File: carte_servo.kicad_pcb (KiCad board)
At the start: 4 copper layers, 185 x 106.7 mm, 134 parts, among them J10 Conn_01x03_Male, J11 Transistor_2, J12 Transistor_1, J13 Transistor_4, J14 Transistor_.3, J16 Conn_01x04_Male, J17 Conn_01x04_Male, J18 Conn_01x03_Male, J19 Conn_01x03_Male, J2 Conn_02x04_Top_Bottom, J20 Stepper, J21 Stepper, J24 Conn_LEDs, J25 Conn_AX12, J29 Conn_AX12, J5 Conn_01x03_Male, J6 Conn_01x03_Male, J7 Conn_01x03_Male, J8 Conn_01x03_Male, J9 Conn_01x03_Male, P1 USB_C_Plug_USB2.0, Q1 DMN2011UTS, Q2 DMN2011UTS, Q3 DMN2011UTS, Q4 DMN2011UTS, Q6 DMN2011UTS, Q7 CSD17307Q5A, Q8 CSD17579Q5A, SW1 CK_KMS2xxG, U1 XGZP6897D_differential_pressu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, U10 TPS563200, U2 XGZP6897D_differential_pressu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, U3 TMC2208_SILENTSTEPSTICK, U4 TMC2208_SILENTSTEPSTICK, U5 74LVC2G241, U6 SN65HVD230, U7 LD1117S33TR_SOT223, U8 ESP32-S3-WROOM-1, U9 LM3150MH

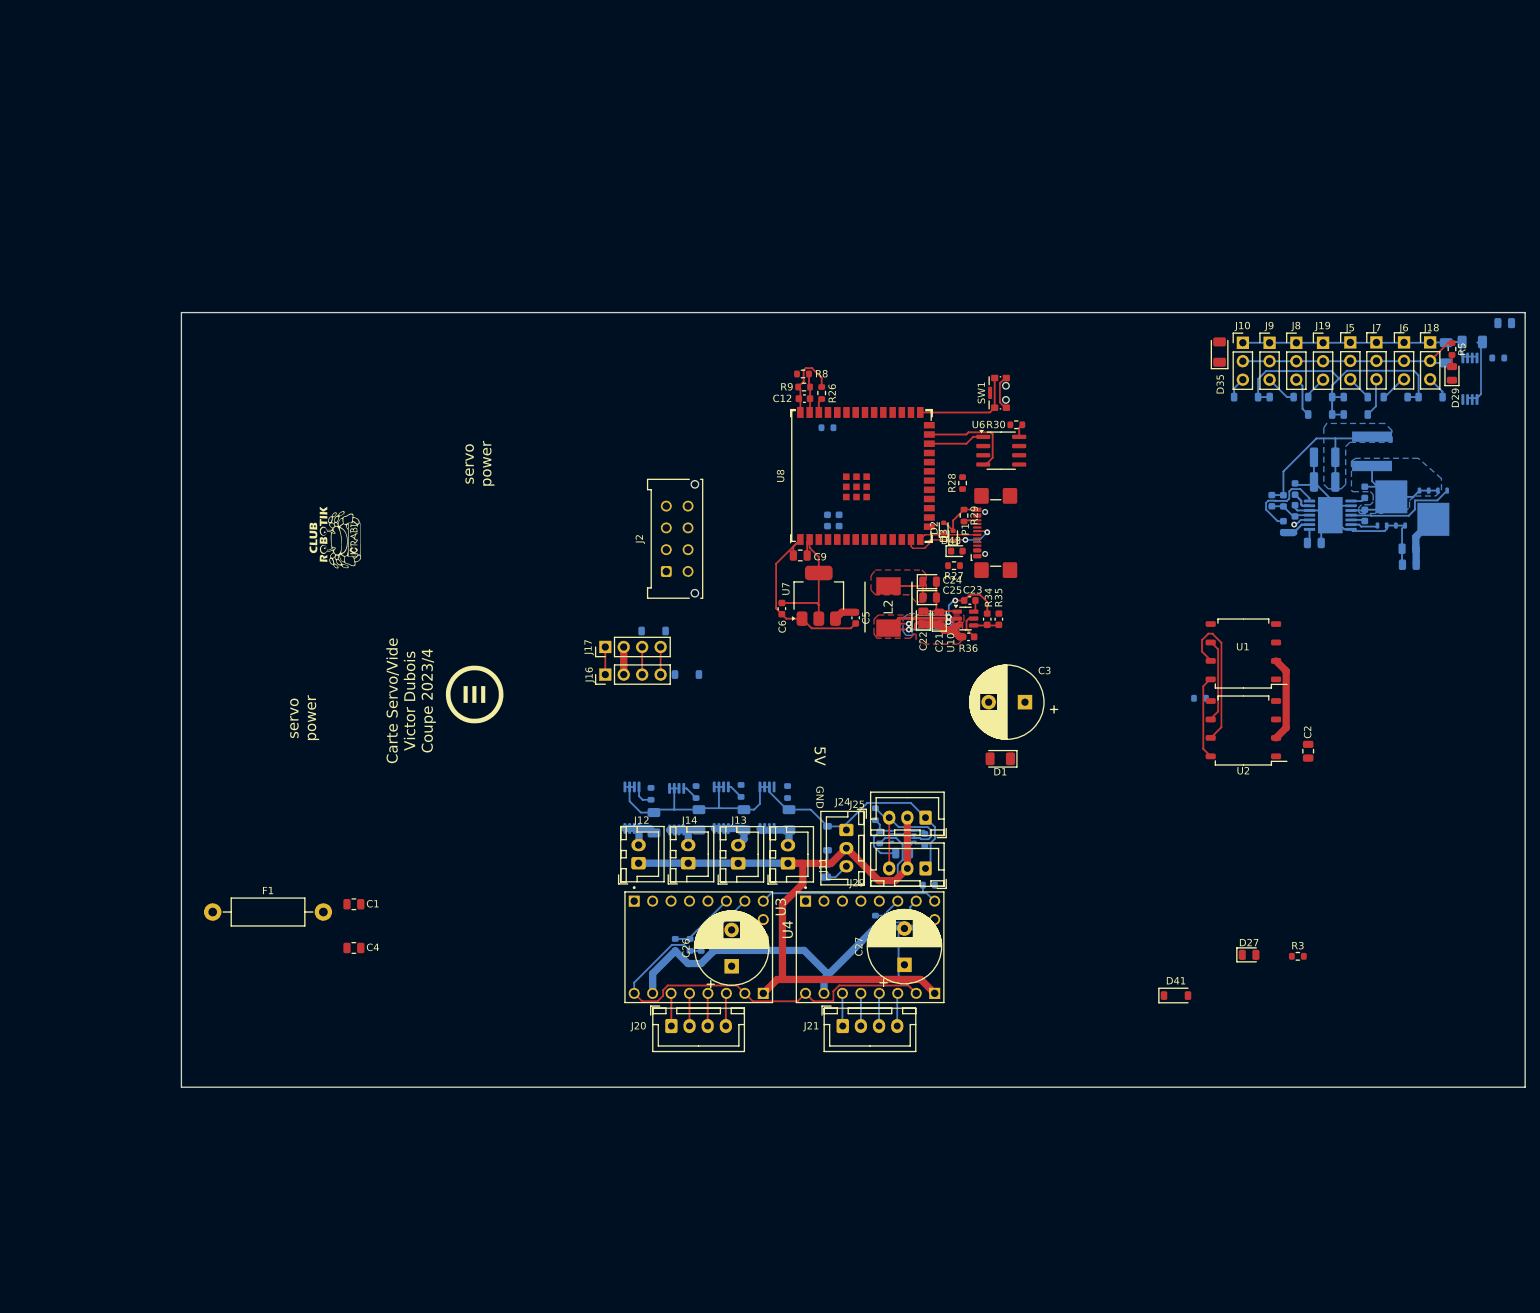
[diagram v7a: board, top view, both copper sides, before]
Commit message: change fuse + start servo order + routing
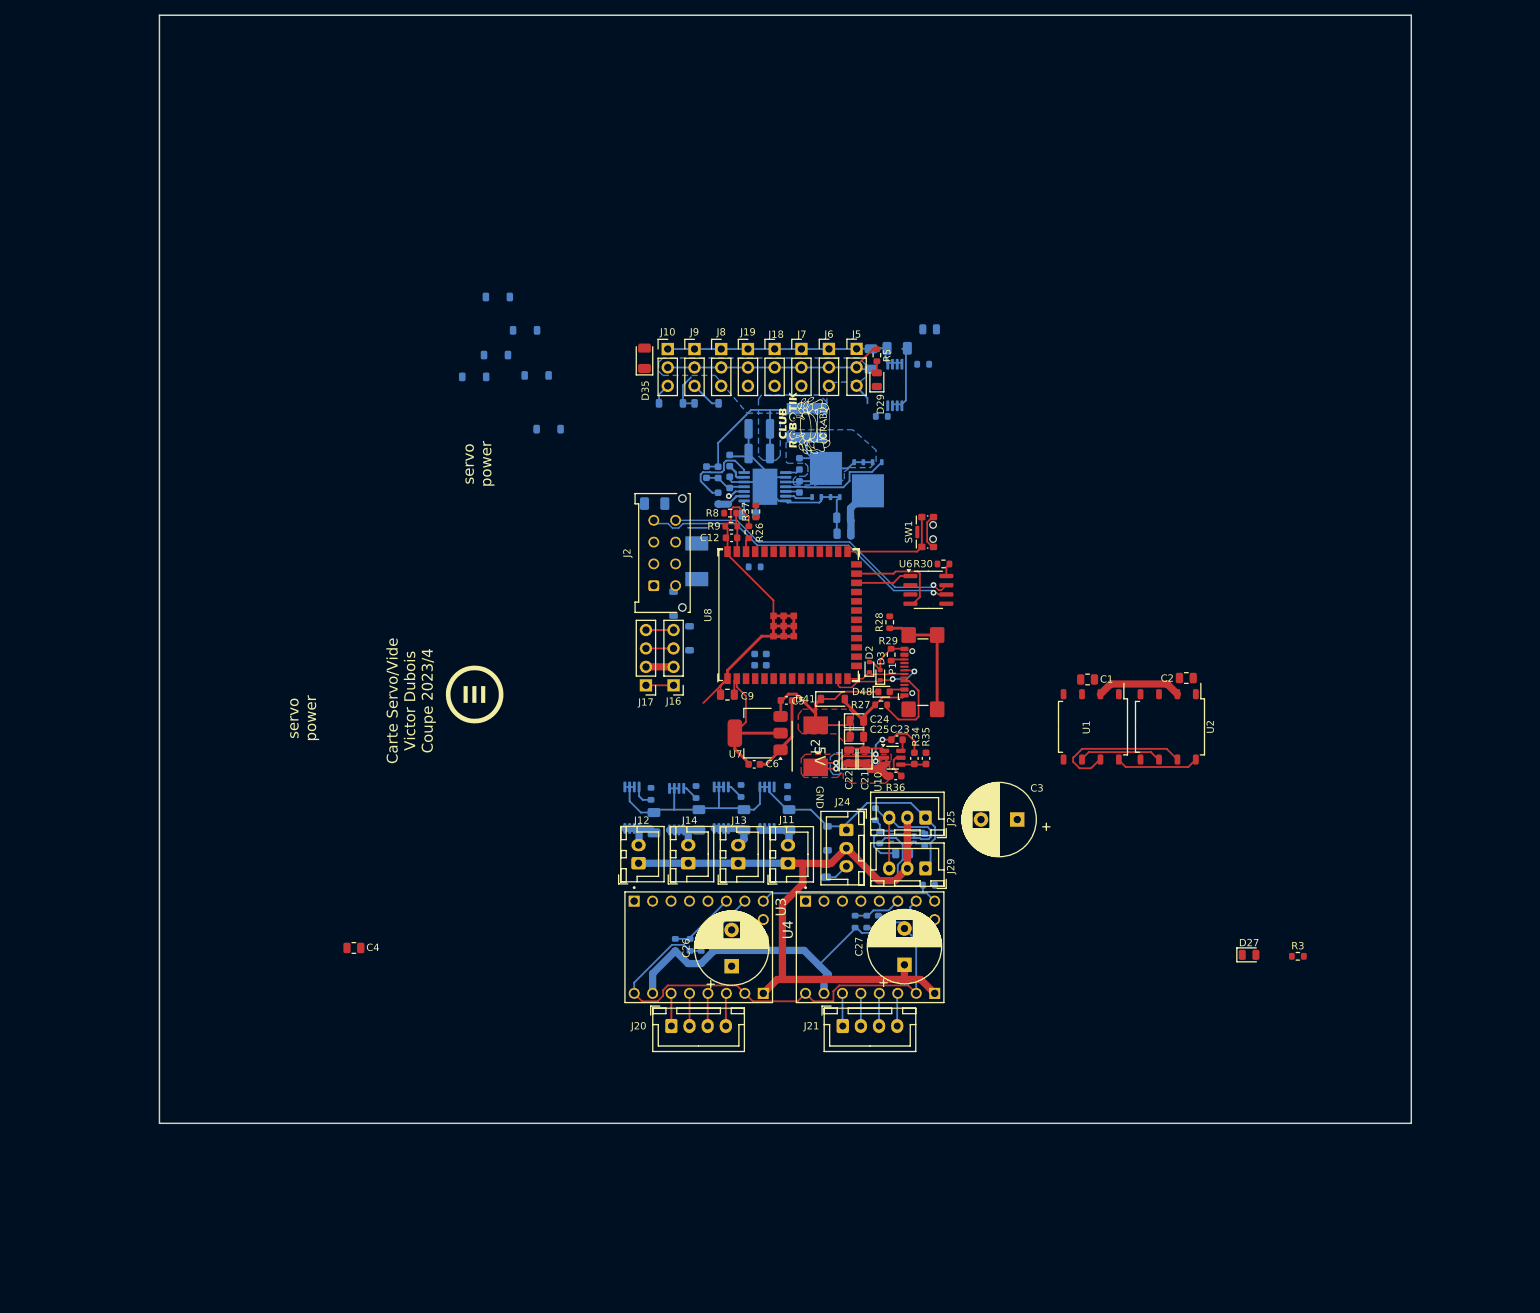
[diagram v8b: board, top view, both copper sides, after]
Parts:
- added R37: 0R, Resistor_SMD:R_0603_1608Metric, F.Cu at (160.1, 85.9)
- D1: moved to B.Cu
- F1: footprint Resistor_THT:R_Axial_DIN0411_L9.9mm_D3.6mm_P15.24mm_Horizontal -> Fuse:Fuse_Littelfuse-NANO2-451_453; moved to B.Cu
- R12: value 0R -> NC
- moved D24 126.9 mm to (121.3, 67.4)
- moved D21 121.5 mm to (131.6, 74.6)
- moved D30 119.3 mm to (124.6, 56.4)
- moved D23 114.8 mm to (128.3, 61.0)
- moved D22 113.6 mm to (124.3, 64.4)
- moved D32 108.0 mm to (129.9, 67.2)
- moved C1 105.7 mm to (205.8, 109.1)
- moved J18 90.3 mm to (162.7, 63.6)
- moved F1 82.3 mm to (152.0, 92.8), turned to 90 degrees
- moved J6 79.2 mm to (170.2, 63.5)
- moved D33 79.2 mm to (153.3, 71.0)
- moved D36 79.2 mm to (148.4, 71.0)
- moved D5 79.2 mm to (179.6, 63.5)
- moved J9 79.2 mm to (151.7, 63.6)
- moved Q6 79.2 mm to (179.3, 68.5)
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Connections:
- net CAN_H renamed CAN+
- net CAN_L renamed CAN-
- J10 pad 3: SERVO_6 -> SERVO_8
- J18 pad 3: SERVO_7 -> SERVO_4
- J19 pad 3: SERVO_8 -> SERVO_5
- J8 pad 3: SERVO_4 -> SERVO_6
- J9 pad 3: SERVO_5 -> SERVO_7
- U8 pad 12: SERVO_1 -> STEP_1
- U8 pad 18: SERVO_2 -> DIR_2
- U8 pad 19: SERVO_3 -> STEP_2
- U8 pad 20: SERVO_7 -> DIR_1
- U8 pad 28: DIR_1 -> SERVO_2
- U8 pad 29: STEP_1 -> SERVO_7
- U8 pad 30: LEDs -> SERVO_3
- U8 pad 31: DIR_2 -> unconnected-(U8-GPIO38/FSPIWP/SUBSPIWP-Pad31)
- U8 pad 34: STEP_2 -> SERVO_1
- U8 pad 37: TRANSISTOR_3 -> SERVO_8
- U8 pad 6: SERVO_8 -> LEDs
- U8 pad 9: SERVO_8 -> TRANSISTOR_3
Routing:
- net CAN-: track 0.00 -> 45.0 mm, vias 0 -> 1
- net CAN+: track 0.00 -> 41.8 mm, vias 0 -> 1
- net Net-(P1-SHIELD): track 0.00 -> 17.1 mm
- net 5V: track 83.3 -> 100.4 mm
- net GND: track 308.9 -> 323.3 mm
- net Net-(P1-CC): track 0.00 -> 11.7 mm
- net /DCDC_5V/SW_DCDC5V: track 40.4 -> 32.4 mm
- net SERVO_4: track 5.48 -> 0.00 mm
- net SERVO_3: track 5.32 -> 0.00 mm
- net BATT_12V: track 110.2 -> 114.8 mm
- net SERVO_2: track 3.61 -> 0.00 mm
- net 3.3V: track 19.0 -> 22.4 mm
- net SERVO_8: track 3.25 -> 0.00 mm
- net SERVO_7: track 3.15 -> 0.00 mm
- net Net-(U4-MS1): track 3.94 -> 6.54 mm
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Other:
- board size 185 x 106.7 mm -> 172.4 x 152.6 mm
